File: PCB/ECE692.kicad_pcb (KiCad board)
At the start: 2 copper layers, 70 x 82.5 mm, 14 parts, among them J1 TYPE-C_16PIN_2MD__073_, J2 Conn_01x12, J3 Screw_Terminal_01x02, J4 Screw_Terminal_01x02, U1 CAN_BUS_TRANSCEIVER1, U2 CAN_BUS_TRANSCEIVER2

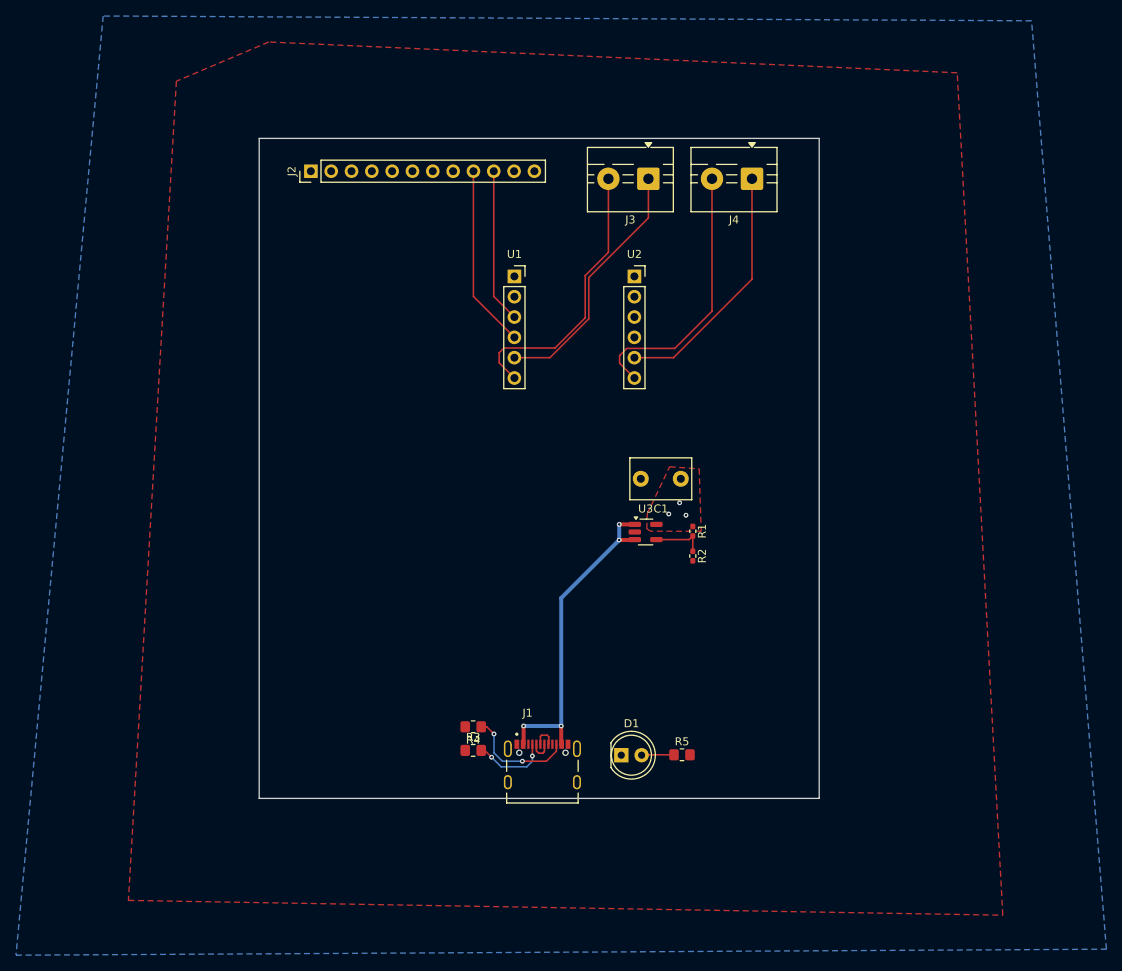
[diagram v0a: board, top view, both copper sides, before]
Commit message: Modified some stuff, and did some routing
- Replaced the rectangle with the STM nucleo board shape
- added the level shifter symbol and footprint
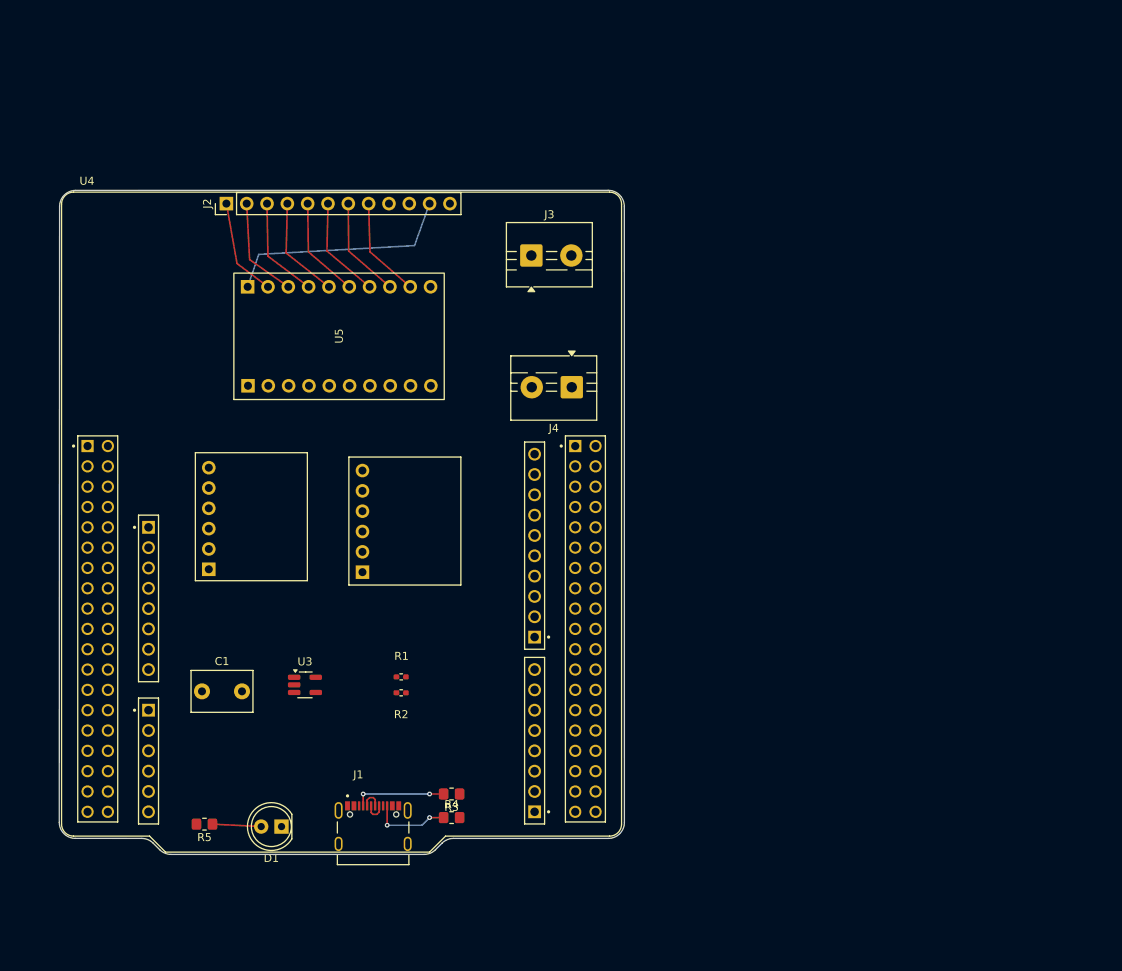
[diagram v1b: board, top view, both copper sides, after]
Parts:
- added U4: STM32F446RETx, NUCLEO-F446RE:MODULE_NUCLEO-F446RE, F.Cu at (116.3, 87.9)
- added U5: LEVEL_SHIFTER, footprints:LEVEL_SHIFTER, F.Cu at (116.0, 64.6)
- U1, U2: moved to B.Cu
- U3: value ~ -> LOD
- moved C1 65.5 mm to (98.8, 109.0), turned to 0 degrees
- moved U2 64.6 mm to (99.7, 93.8)
- moved R5 60.3 mm to (99.2, 125.6), turned to 180 degrees
- moved U3 46.7 mm to (111.7, 108.2)
- moved D1 43.4 mm to (108.8, 125.9), turned to 180 degrees
- moved U1 41.6 mm to (118.9, 94.1)
- moved R1 40.7 mm to (123.8, 107.2), turned to 180 degrees
- moved R2 40.3 mm to (123.8, 109.2), turned to 0 degrees
- moved J4 34.4 mm to (145.1, 71.0)
- moved J1 22.5 mm to (120.2, 127.0)
- moved J3 17.5 mm to (140.0, 54.5), turned to 0 degrees
- moved R4 11.7 mm to (130.1, 124.8), turned to 0 degrees
- moved J2 11.3 mm to (101.9, 48.0)
- moved R3 6.08 mm to (130.1, 121.8), turned to 180 degrees
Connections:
- J4 pad 1: Net-(J4-Pin_1) -> Net-(J3-Pin_1)
- J4 pad 2: Net-(J4-Pin_2) -> Net-(J3-Pin_2)
- U2 pad 5: Net-(J4-Pin_1) -> Net-(J3-Pin_1)
- U2 pad 6: Net-(J4-Pin_2) -> Net-(J3-Pin_2)
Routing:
- net VBUS: track 41.4 -> 0.00 mm, vias 4 -> 0
- net Net-(J3-Pin_2): track 35.1 -> 0.00 mm
- net Net-(J4-Pin_2): track 34.0 -> 0.00 mm
- net Net-(J3-Pin_1): track 31.9 -> 0.00 mm
- net Net-(J4-Pin_1): track 31.3 -> 0.00 mm
- net V_TB: track 0.00 -> 29.4 mm
- net CTX_TB: track 22.9 -> 0.00 mm
- net CRX_TB: track 19.3 -> 0.00 mm
- net TB_CH4: track 0.00 -> 13.0 mm
- net TB_CH3: track 0.00 -> 12.9 mm
- net TB_CH2: track 0.00 -> 12.9 mm
- net TB_CH6: track 0.00 -> 12.9 mm
- net TB_CH7: track 0.00 -> 12.8 mm
- net TB_CH5: track 0.00 -> 12.8 mm
- net TB_CH8: track 0.00 -> 12.7 mm
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- removed copper zone on B.Cu, net 3V3
- removed copper zone on F.Cu, net 3V3
- removed copper zone on F.Cu, net GND
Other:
- board size 70 x 82.5 mm -> 70.6 x 83 mm

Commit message: Finished the PCB
- Finished the PCB and ordered at JLCPCB
- Uploaded schematic pdf, and image of complete layout and routing
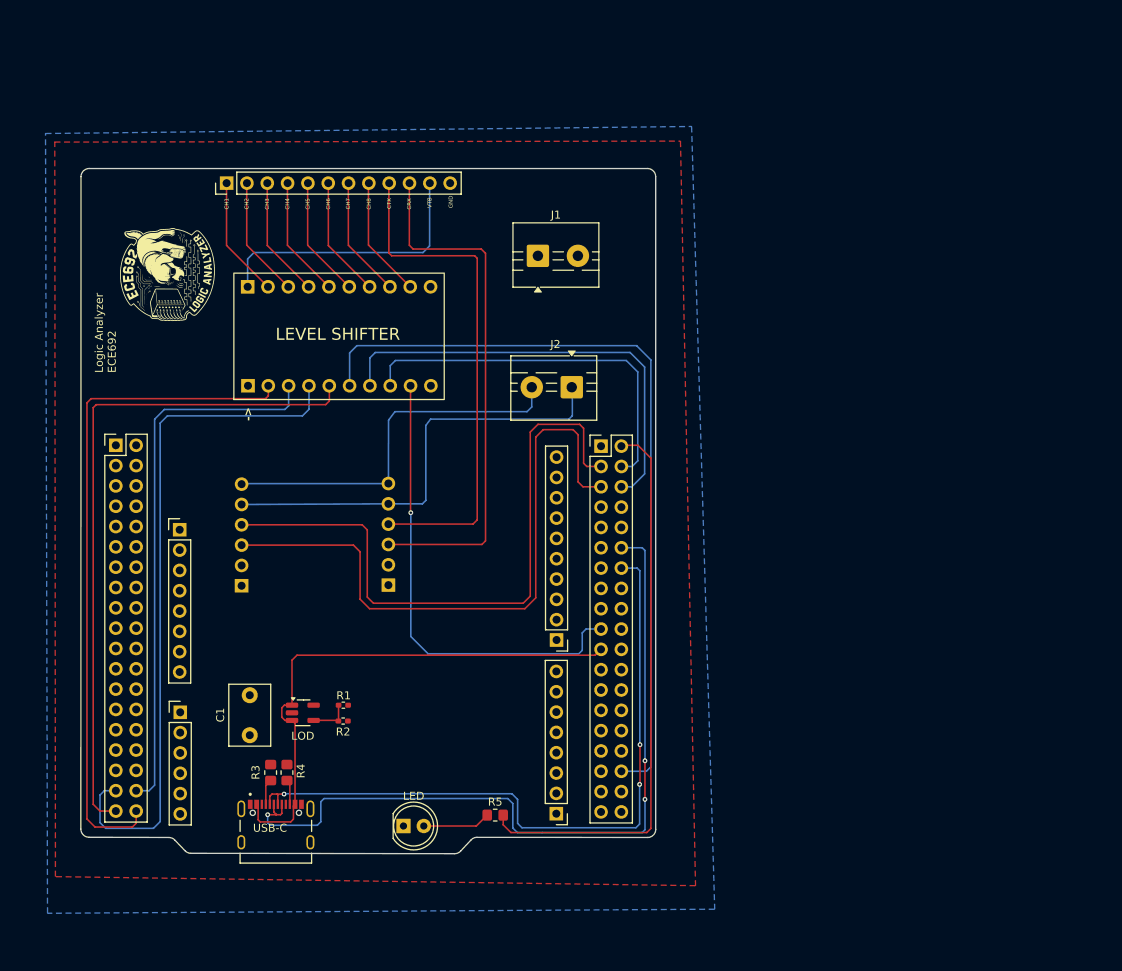
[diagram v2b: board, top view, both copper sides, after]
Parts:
- removed the U4 at (116.3, 87.9)
- added G***: LOGO, footprints:Logo_v3_new, F.Cu at (94.5, 56.9)
- added REF**: PinHeader_1x10_P2.54mm_Vertical, Connector_PinHeader_2.54mm:PinHeader_1x10_P2.54mm_Vertical, F.Cu at (143.2, 102.6)
- added REF**: PinHeader_1x08_P2.54mm_Vertical, Connector_PinHeader_2.54mm:PinHeader_1x08_P2.54mm_Vertical, F.Cu at (96.1, 88.8)
- added REF**: PinHeader_1x08_P2.54mm_Vertical, Connector_PinHeader_2.54mm:PinHeader_1x08_P2.54mm_Vertical, F.Cu at (143.1, 124.3)
- added REF**: PinHeader_1x06_P2.54mm_Vertical, Connector_PinHeader_2.54mm:PinHeader_1x06_P2.54mm_Vertical, F.Cu at (96.1, 111.6)
- added U5: NUCLEO-F446RE, Connector_PinHeader_2.54mm:PinHeader_2x19_P2.54mm_Vertical, F.Cu at (88.1, 78.3)
- added U6: NUCLEO-F446RE, Connector_PinHeader_2.54mm:PinHeader_2x19_P2.54mm_Vertical, F.Cu at (148.7, 78.4)
- moved R5 36.4 mm to (135.5, 124.5), turned to 0 degrees
- moved R3 22.8 mm to (107.4, 119.2), turned to -90 degrees
- moved R4 21.3 mm to (109.5, 119.2), turned to 90 degrees
- moved D1 15.2 mm to (124.0, 125.8), turned to 0 degrees
- moved J1 12.2 mm to (108.1, 126.8)
- moved R2 8.07 mm to (116.5, 112.7)
- moved R1 8.05 mm to (116.5, 110.8)
- moved C1 5.99 mm to (104.8, 109.5), turned to -90 degrees
- moved U2 4.59 mm to (103.8, 95.8)
- moved U1 3.62 mm to (122.2, 95.7)
- moved U3 3.50 mm to (111.5, 111.7)
- moved J2 2.56 mm to (101.9, 45.5)
- moved J1 0.82 mm to (140.8, 54.6)
- renumbered J3 to J1, J4 to J2, U5 to U4
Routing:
- net CH5: track 0.00 -> 97.7 mm
- net D+: track 2.82 -> 97.4 mm, vias 0 -> 3
- net CH3: track 0.00 -> 85.9 mm
- net CH1: track 0.00 -> 84.6 mm
- net CH4: track 0.00 -> 84.5 mm
- net D-: track 2.76 -> 86.5 mm, vias 0 -> 3
- net CRX: track 0.00 -> 79.9 mm
- net CTX: track 0.00 -> 79.2 mm
- net Net-(U6B-PC8): track 0.00 -> 71.0 mm
- net CH2: track 0.00 -> 68.3 mm
- net VBUS: track 0.00 -> 68.2 mm
- net CRX_TB: track 0.00 -> 66.0 mm
- net CTX_TB: track 0.00 -> 64.1 mm
- net CH8: track 0.00 -> 58.6 mm, vias 0 -> 1
- net CH6: track 0.00 -> 55.8 mm
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- added copper zone on F.Cu, net 3V3
- added copper zone on B.Cu, net GND
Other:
- board size 70.6 x 83 mm -> 71.9 x 85.6 mm
- board text added: "->"
- board text added: "CH1"
- board text added: "CH2"
- board text added: "CH3"
- board text added: "CH4"
- board text added: "CH5"
- board text added: "CH6"
- board text added: "CH7"
- board text added: "CH8"
- board text added: "CRX"
- board text added: "CT A"
- board text added: "CT B"
- board text added: "CTX"
- board text added: "GND"
- board text added: "LEVEL SHIFTER"
- board text added: "Logic Analyzer ECE692"
- board text added: "USB-C"
- board text added: "VTB"
